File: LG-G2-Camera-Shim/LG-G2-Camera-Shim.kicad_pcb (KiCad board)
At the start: 2 copper layers, 19.8 x 10.2 mm, 4 parts, among them P1 LG-G2-G3-Rear-Camera, P2 CONN_02X02, P3 CONN_01X03, P4 LG-G2-G3-Rear-Camera

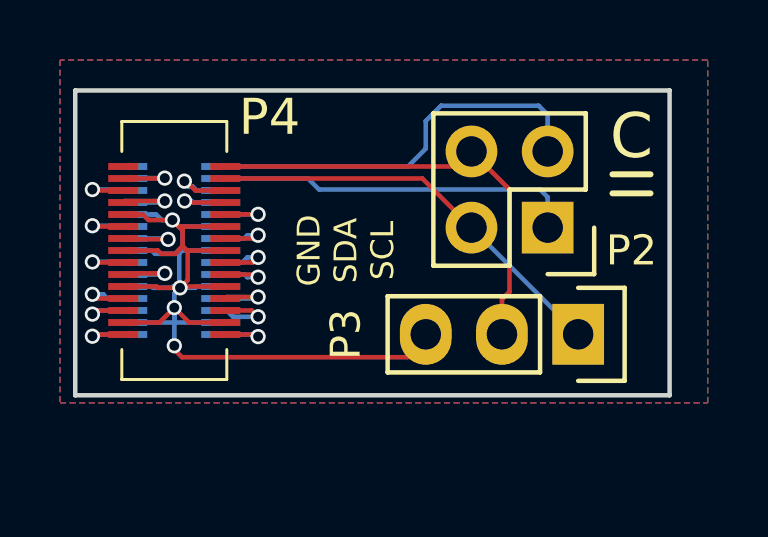
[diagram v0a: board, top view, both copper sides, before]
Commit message: Redraw shim for improved manufacturability
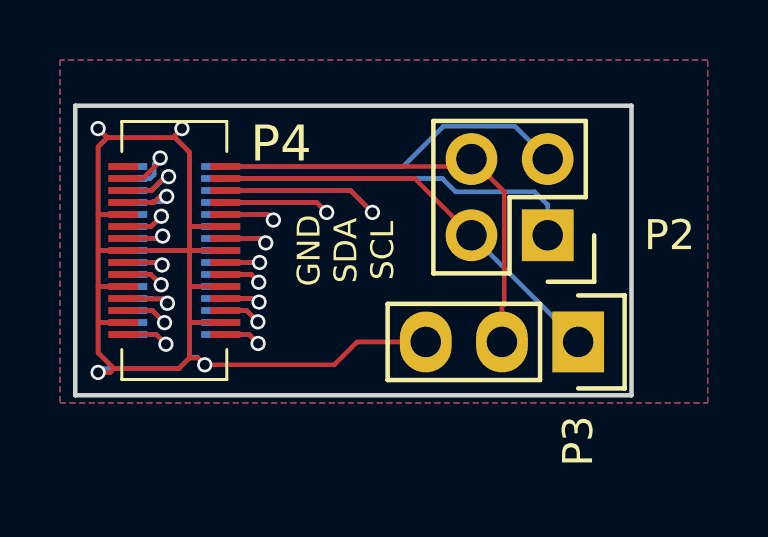
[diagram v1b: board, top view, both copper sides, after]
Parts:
- moved P3 0.25 mm to (159.5, 111.0)
- moved P2 0.25 mm to (158.5, 107.4)
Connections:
- net /CAM_SCL_IN renamed /PHONE_SCL
- net /CAM_SCL_OUT renamed /CAM_SCL
- net /CAM_SDA_IN renamed /PHONE_SDA
- net /CAM_SDA_OUT renamed /CAM_SDA
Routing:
- net GND: track 41.3 -> 73.1 mm
- net /+1V0_VREG_L3: track 2.56 -> 10.9 mm
- net /+1V8_13M_VDDIO: track 2.31 -> 7.48 mm
- net /PHONE_SDA: track 13.9 -> 12.2 mm
- net /CAM_RESET_N: track 2.64 -> 3.81 mm
- net /CAM_MCLK: track 2.73 -> 3.27 mm
- net /OIS_RESET_N: track 2.33 -> 2.84 mm
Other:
- board size 19.8 x 10.2 mm -> 18.5 x 9.7 mm
- board text removed: "C"
